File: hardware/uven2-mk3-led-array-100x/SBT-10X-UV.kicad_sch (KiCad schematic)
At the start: 3 parts

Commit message: more layout
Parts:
- renumbered C75 to C177, C76 to C178, D38 to D89

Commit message: more layout
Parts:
- renumbered C177 to C21, C178 to C22, D89 to D11

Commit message: layout almost finished
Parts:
- renumbered C21 to C15, C22 to C16, D11 to D8

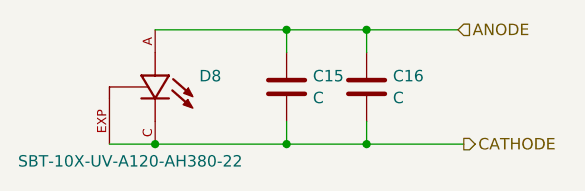
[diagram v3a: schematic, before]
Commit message: added direct heat sink pad of leds
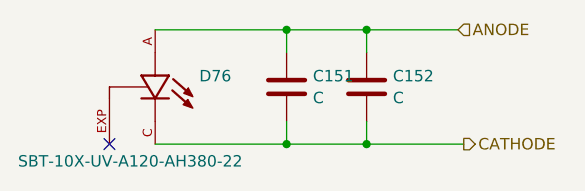
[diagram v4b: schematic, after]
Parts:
- renumbered C15 to C151, C16 to C152, D8 to D76
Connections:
- net CATHODE: no longer D76.EXP
- no-connect marks 0 -> 1
